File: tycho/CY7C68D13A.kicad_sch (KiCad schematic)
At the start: 23 parts, among them U1 CY7C68013A-56LTX, U2 MIC5504-3.3YM5, Y1 24 MHz

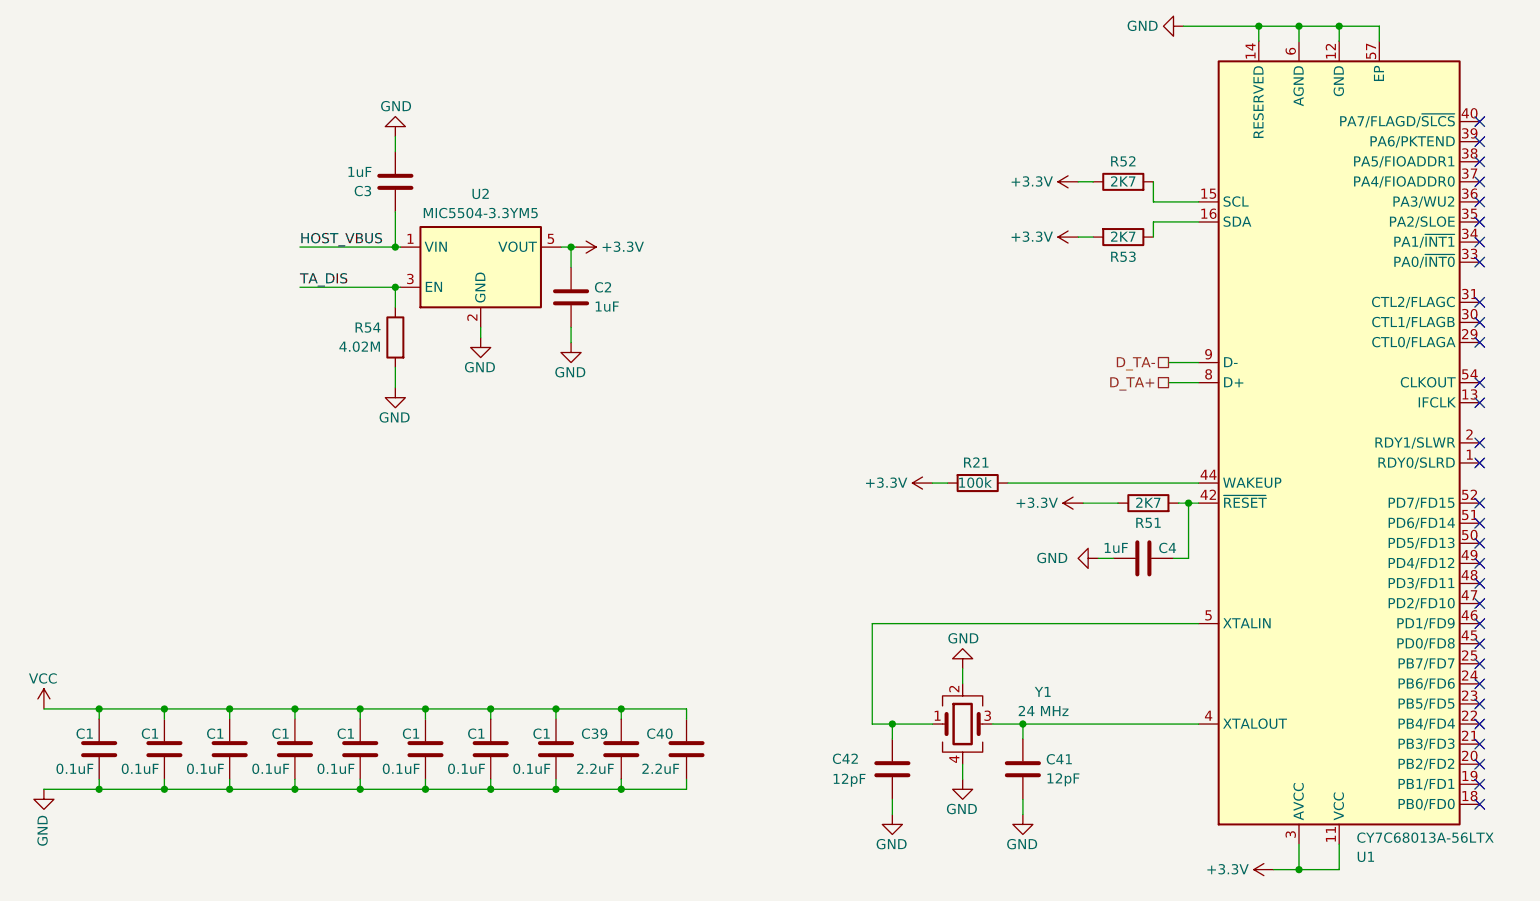
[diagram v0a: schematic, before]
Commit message: Add EEPROM chip; move signals
	*Add EEPROM chip to Cypress FX2to hold firmware
	*Move SIG2_S signal from J2_P27 to J2_P26
	*Move BOOST_EN signal from J2_P26 to J2_P25
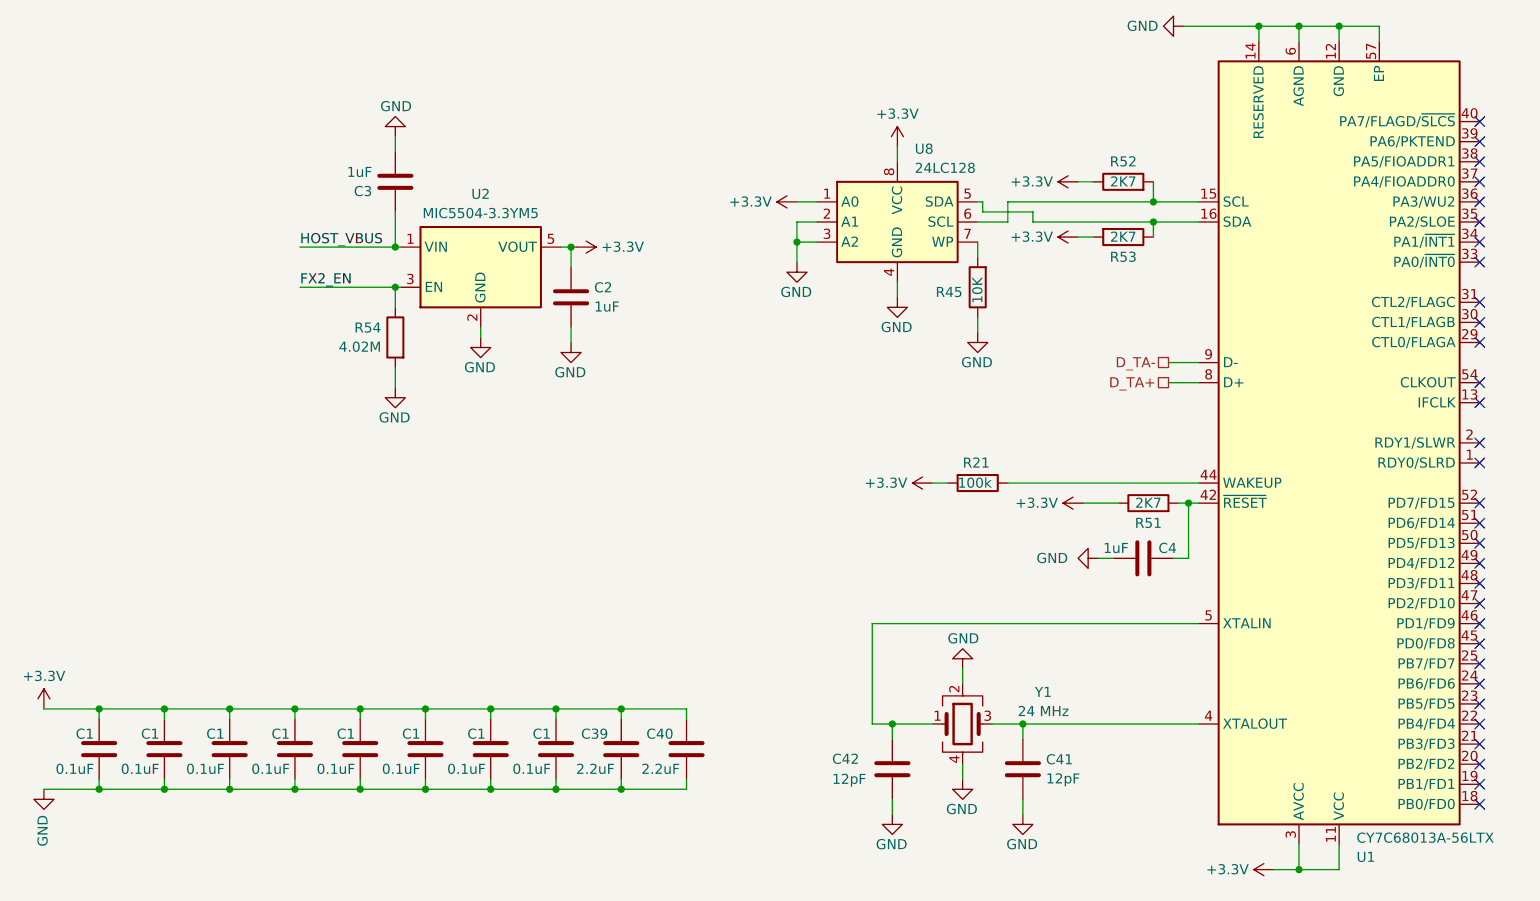
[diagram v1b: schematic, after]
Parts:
- added R45: 10K, Resistor_SMD:R_0603_1608Metric_Pad0.98x0.95mm_HandSolder, symbol Device:R
- added U8: 24LC128, Package_SO:SOIC-8_3.9x4.9mm_P1.27mm, symbol Memory_EEPROM:24LC128
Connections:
- net VCC is gone; now on net +3.3V: C1.1, C1.1, C1.1, C1.1, C1.1, C1.1, C1.1, C1.1, C39.1, C40.1
- net +3.3V: now also U8.1 (A0), U8.8 (VCC)
- net GND: now also R45.1, U8.2 (A1), U8.3 (A2), U8.4 (GND)
- net at R52.2, U1.15 (SCL): now also U8.6 (SCL)
- net at R53.1, U1.16 (SDA): now also U8.5 (SDA)
- net TA_DIS renamed FX2_EN
- new net: R45.2, U8.7 (WP)

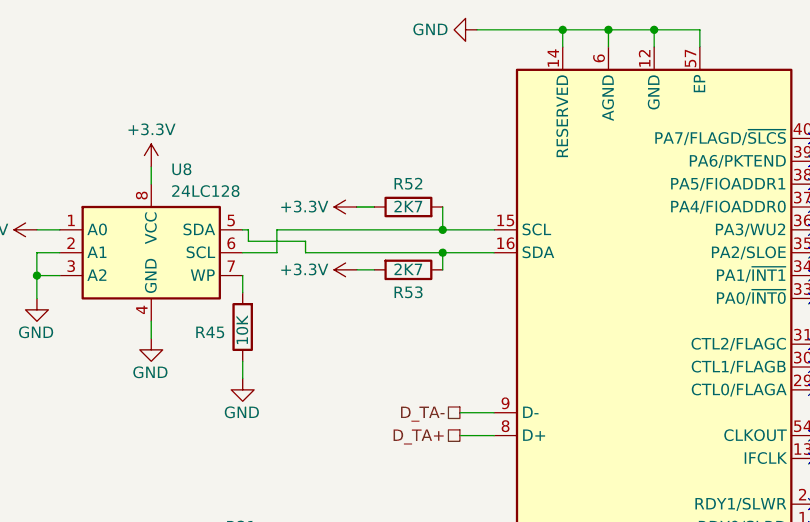
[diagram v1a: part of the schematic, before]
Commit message: Update SDA/SCL pull-up resistor values
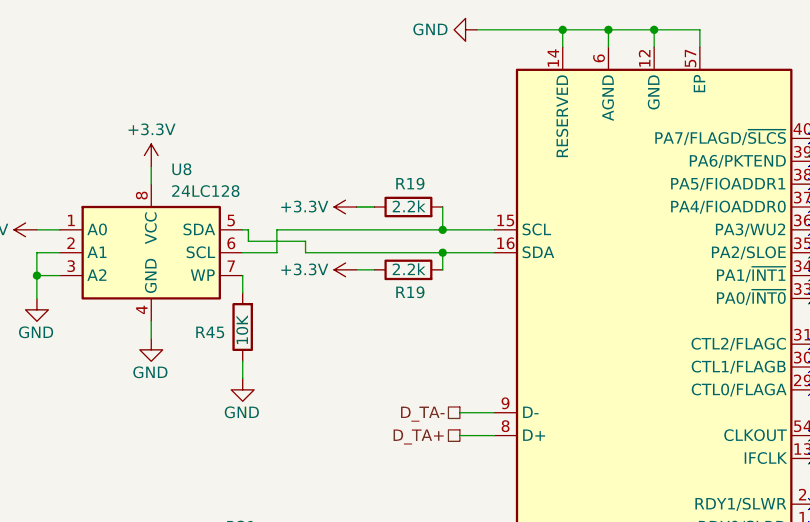
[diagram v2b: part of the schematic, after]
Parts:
- removed R52, R53: 2K7, Resistor_SMD:R_0603_1608Metric_Pad0.98x0.95mm_HandSolder, symbol Device:R
- added R19 (x2): 2.2k, Resistor_SMD:R_0402_1005Metric_Pad0.72x0.64mm_HandSolder, symbol Device:R
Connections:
- net +3.3V: now also R19.1, R19.1
- net at U1.16 (SDA), U8.5 (SDA): now also R19.2
- net at U1.15 (SCL), U8.6 (SCL): now also R19.2
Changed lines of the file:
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@@
-    )
-  )
-  (symbol (lib_id "Device:R") (at 201.295 59.69 90) (unit 1)
-    (in_bom yes) (on_board yes) (dnp no)
-    (property "Reference" "R52" (at 201.295 57.15 90)
-      (effects (font (size 1.27 1.27)))
-    )
-    (property "Value" "2K7" (at 201.295 59.69 90)
-      (effects (font (size 1.27 1.27)))
-    )
-    (property "Footprint" "Resistor_SMD:R_0603_1608Metric_Pad0.98x0.95mm_HandSolder" (at 201.295 61.468 90)
-      (effects (font (size 1.27 1.27)) hide)
-    )
-    (property "Datasheet" "~" (at 201.295 59.69 0)
-      (effects (font (size 1.27 1.27)) hide)
-    )
-    (property "Manufacturer" "YAGEO" (at 201.295 59.69 0)
-      (effects (font (size 1.27 1.27)) hide)
-    )
-    (property "Part Number" "RC0603DR-072K7L" (at 201.295 59.69 0)
-      (effects (font (size 1.27 1.27)) hide)
-    )
-    (property "Description" "100mW Thick Film Resistors ±100ppm/℃ ±0.5% 2.7kΩ 0603  Chip Resistor - Surface Mount ROHS" (at 201.295 59.69 0)
-      (effects (font (size 1.27 1.27)) hide)
-    )
-    (pin "1")
-    (pin "2")
-    (instances
-      (project "tycho"
-        (path "/4ed1cbaf-15e8-40e5-8366-86487d525fd5"
-          (reference "R52") (unit 1)
-        )
-        (path "/4ed1cbaf-15e8-40e5-8366-86487d525fd5/b3c8fc2b-e9c9-4d47-a73a-55bc7ffe8734"
-          (reference "R51") (unit 1)
-        )
-      )
     )
   )
@@
         (path "/4ed1cbaf-15e8-40e5-8366-86487d525fd5/b3c8fc2b-e9c9-4d47-a73a-55bc7ffe8734"
           (reference "C6") (unit 1)
+        )
+      )
+    )
+  )
+  (symbol (lib_id "Device:R") (at 201.295 66.675 90) (unit 1)
+    (in_bom yes) (on_board yes) (dnp no)
+    (property "Reference" "R19" (at 203.2 69.215 90)
+      (effects (font (size 1.27 1.27)) (justify left))
+    )
+    (property "Value" "2.2k" (at 203.2 66.675 90)
+      (effects (font (size 1.27 1.27)) (justify left))
+    )
+    (property "Footprint" "Resistor_SMD:R_0402_1005Metric_Pad0.72x0.64mm_HandSolder" (at 201.295 68.453 90)
+      (effects (font (size 1.27 1.27)) hide)
+    )
+    (property "Datasheet" "~" (at 201.295 66.675 0)
+      (effects (font (size 1.27 1.27)) hide)
+    )
+    (property "Manufacturer" "Vishay Dale" (at 201.295 66.675 0)
+      (effects (font (size 1.27 1.27)) hide)
+    )
+    (property "Part Number" "CRCW04022K20FKED" (at 201.295 66.675 0)
+      (effects (font (size 1.27 1.27)) hide)
+    )
+    (property "Description" "RES SMD 2.2K OHM 1% 1/16W 0402" (at 201.295 66.675 0)
+      (effects (font (size 1.27 1.27)) hide)
+    )
+    (property "Substitution" "any equivalent" (at 201.295 66.675 0)
+      (effects (font (size 1.27 1.27)) hide)
+    )
+    (pin "1")
+    (pin "2")
+    (instances
+      (project "tycho"
+        (path "/4ed1cbaf-15e8-40e5-8366-86487d525fd5/175ec40e-e1eb-4798-86e4-603e661ed6e0"
+          (reference "R19") (unit 1)
+        )
+        (path "/4ed1cbaf-15e8-40e5-8366-86487d525fd5/b3c8fc2b-e9c9-4d47-a73a-55bc7ffe8734"
+          (reference "R52") (unit 1)
         )
       )
@@
     )
   )
-  (symbol (lib_id "Device:R") (at 201.295 66.675 270) (unit 1)
-    (in_bom yes) (on_board yes) (dnp no)
-    (property "Reference" "R53" (at 201.295 69.215 90)
-      (effects (font (size 1.27 1.27)))
-    )
-    (property "Value" "2K7" (at 201.295 66.675 90)
-      (effects (font (size 1.27 1.27)))
-    )
-    (property "Footprint" "Resistor_SMD:R_0603_1608Metric_Pad0.98x0.95mm_HandSolder" (at 201.295 64.897 90)
-      (effects (font (size 1.27 1.27)) hide)
-    )
-    (property "Datasheet" "~" (at 201.295 66.675 0)
-      (effects (font (size 1.27 1.27)) hide)
-    )
-    (property "Manufacturer" "YAGEO" (at 201.295 66.675 0)
-      (effects (font (size 1.27 1.27)) hide)
-    )
-    (property "Part Number" "RC0603DR-072K7L" (at 201.295 66.675 0)
-      (effects (font (size 1.27 1.27)) hide)
-    )
-    (property "Description" "100mW Thick Film Resistors ±100ppm/℃ ±0.5% 2.7kΩ 0603  Chip Resistor - Surface Mount ROHS" (at 201.295 66.675 0)
-      (effects (font (size 1.27 1.27)) hide)
-    )
-    (pin "1")
-    (pin "2")
-    (instances
-      (project "tycho"
-        (path "/4ed1cbaf-15e8-40e5-8366-86487d525fd5"
-          (reference "R53") (unit 1)
-        )
-        (path "/4ed1cbaf-15e8-40e5-8366-86487d525fd5/b3c8fc2b-e9c9-4d47-a73a-55bc7ffe8734"
-          (reference "R52") (unit 1)
-        )
-      )
-    )
-  )
   (symbol (lib_id "Device:C") (at 188.595 133.985 0) (unit 1)
     (in_bom yes) (on_board yes) (dnp no) (fields_autoplaced)
@@
         )
       )
+    )
+  )
+  (symbol (lib_id "Device:R") (at 201.295 59.69 90) (unit 1)
+    (in_bom yes) (on_board yes) (dnp no)
+    (property "Reference" "R19" (at 203.2 57.15 90)
+      (effects (font (size 1.27 1.27)) (justify left))
+    )
+    (property "Value" "2.2k" (at 203.2 59.69 90)
+      (effects (font (size 1.27 1.27)) (justify left))
+    )
+    (property "Footprint" "Resistor_SMD:R_0402_1005Metric_Pad0.72x0.64mm_HandSolder" (at 201.295 61.468 90)
+      (effects (font (size 1.27 1.27)) hide)
+    )
+    (property "Datasheet" "~" (at 201.295 59.69 0)
+      (effects (font (size 1.27 1.27)) hide)
+    )
+    (property "Manufacturer" "Vishay Dale" (at 201.295 59.69 0)
+      (effects (font (size 1.27 1.27)) hide)
+    )
+    (property "Part Number" "CRCW04022K20FKED" (at 201.295 59.69 0)
+      (effects (font (size 1.27 1.27)) hide)
+    )
+    (property "Description" "RES SMD 2.2K OHM 1% 1/16W 0402" (at 201.295 59.69 0)
+      (effects (font (size 1.27 1.27)) hide)
+    )
+    (property "Substitution" "any equivalent" (at 201.295 59.69 0)
+      (effects (font (size 1.27 1.27)) hide)
+    )
+    (pin "1")
+    (pin "2")
+    (instances
+      (project "tycho"
+        (path "/4ed1cbaf-15e8-40e5-8366-86487d525fd5/175ec40e-e1eb-4798-86e4-603e661ed6e0"
+          (reference "R19") (unit 1)
+        )
+        (path "/4ed1cbaf-15e8-40e5-8366-86487d525fd5/b3c8fc2b-e9c9-4d47-a73a-55bc7ffe8734"
+          (reference "R51") (unit 1)
+        )
+      )

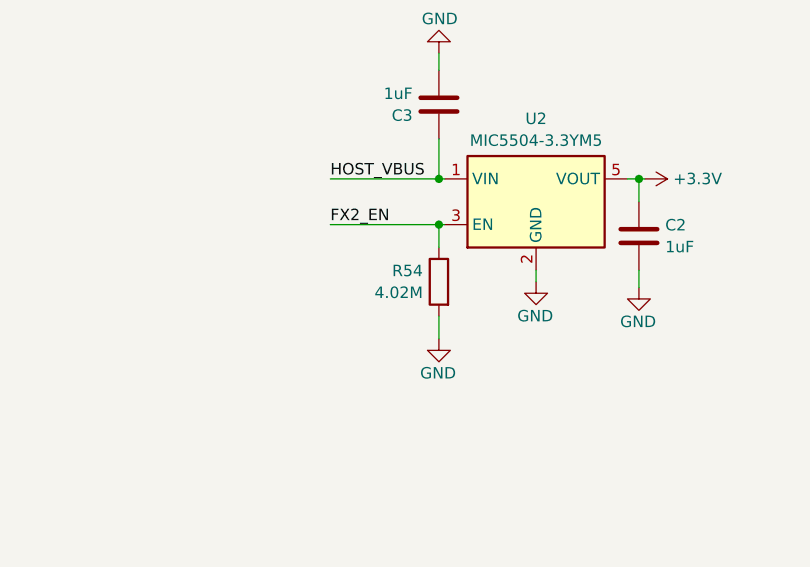
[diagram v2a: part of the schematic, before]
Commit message: Change value of R54 to 10k
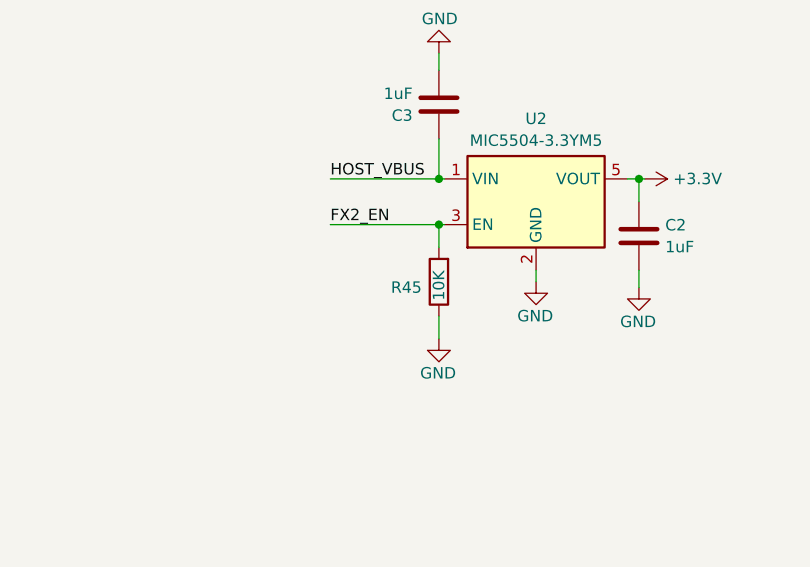
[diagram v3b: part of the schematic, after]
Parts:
- removed R54: 4.02M, Resistor_SMD:R_0603_1608Metric_Pad0.98x0.95mm_HandSolder, symbol Device:R
- added R45: 10K, Resistor_SMD:R_0603_1608Metric_Pad0.98x0.95mm_HandSolder, symbol Device:R
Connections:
- net FX2_EN: now also R45.2
- net GND: now also R45.1
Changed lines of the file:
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@@
-    )
-  )
-  (symbol (lib_id "Device:R") (at 109.22 79.375 0) (mirror y) (unit 1)
-    (in_bom yes) (on_board yes) (dnp no)
-    (property "Reference" "R54" (at 107.442 78.1629 0)
-      (effects (font (size 1.27 1.27)) (justify left))
-    )
-    (property "Value" "4.02M" (at 107.442 80.5871 0)
-      (effects (font (size 1.27 1.27)) (justify left))
-    )
-    (property "Footprint" "Resistor_SMD:R_0603_1608Metric_Pad0.98x0.95mm_HandSolder" (at 110.998 79.375 90)
-      (effects (font (size 1.27 1.27)) hide)
-    )
-    (property "Datasheet" "~" (at 109.22 79.375 0)
-      (effects (font (size 1.27 1.27)) hide)
-    )
-    (property "Manufacturer" "YAGEO" (at 109.22 79.375 0)
-      (effects (font (size 1.27 1.27)) hide)
-    )
-    (property "Part Number" "RC0603FR-074M02L" (at 109.22 79.375 0)
-      (effects (font (size 1.27 1.27)) hide)
-    )
-    (property "Description" "100mW Thick Film Resistors ±100ppm/℃ ±1% 4.02MΩ 0603  Chip Resistor - Surface Mount ROHS" (at 109.22 79.375 0)
-      (effects (font (size 1.27 1.27)) hide)
-    )
-    (pin "1")
-    (pin "2")
-    (instances
-      (project "tycho"
-        (path "/4ed1cbaf-15e8-40e5-8366-86487d525fd5/b3c8fc2b-e9c9-4d47-a73a-55bc7ffe8734"
-          (reference "R54") (unit 1)
-        )
-      )
     )
   )
@@
         )
       )
+    )
+  )
+  (symbol (lib_id "Device:R") (at 109.22 79.375 180) (unit 1)
+    (in_bom yes) (on_board yes) (dnp no)
+    (property "Reference" "R45" (at 107.315 80.01 0)
+      (effects (font (size 1.27 1.27)) (justify left))
+    )
+    (property "Value" "10K" (at 109.22 78.105 90)
+      (effects (font (size 1.27 1.27)) (justify left))
+    )
+    (property "Footprint" "Resistor_SMD:R_0603_1608Metric_Pad0.98x0.95mm_HandSolder" (at 110.998 79.375 90)
+      (effects (font (size 1.27 1.27)) hide)
+    )
+    (property "Datasheet" "~" (at 109.22 79.375 0)
+      (effects (font (size 1.27 1.27)) hide)
+    )
+    (property "Part Number" "RNCP0603FTD10K0" (at 109.22 79.375 0)
+      (effects (font (size 1.27 1.27)) hide)
+    )
+    (property "Substitution" "any equivalent" (at 109.22 79.375 0)
+      (effects (font (size 1.27 1.27)) hide)
+    )
+    (property "Manufacturer" "Stackpole Electronics Inc" (at 109.22 79.375 0)
+      (effects (font (size 1.27 1.27)) hide)
+    )
+    (property "Description" "RES 10K OHM 1% 1/8W 0603" (at 109.22 79.375 0)
+      (effects (font (size 1.27 1.27)) hide)
+    )
+    (pin "1")
+    (pin "2")
+    (instances
+      (project "tycho"
+        (path "/4ed1cbaf-15e8-40e5-8366-86487d525fd5/adaa3f42-a370-4a4c-b378-51d1ea5352f8"
+          (reference "R45") (unit 1)
+        )
+        (path "/4ed1cbaf-15e8-40e5-8366-86487d525fd5"
+          (reference "R3") (unit 1)
+        )
+        (path "/4ed1cbaf-15e8-40e5-8366-86487d525fd5/b3c8fc2b-e9c9-4d47-a73a-55bc7ffe8734"
+          (reference "R54") (unit 1)
+        )
+      )
